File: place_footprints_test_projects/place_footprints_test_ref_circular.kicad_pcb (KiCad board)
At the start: 2 copper layers, 65 parts

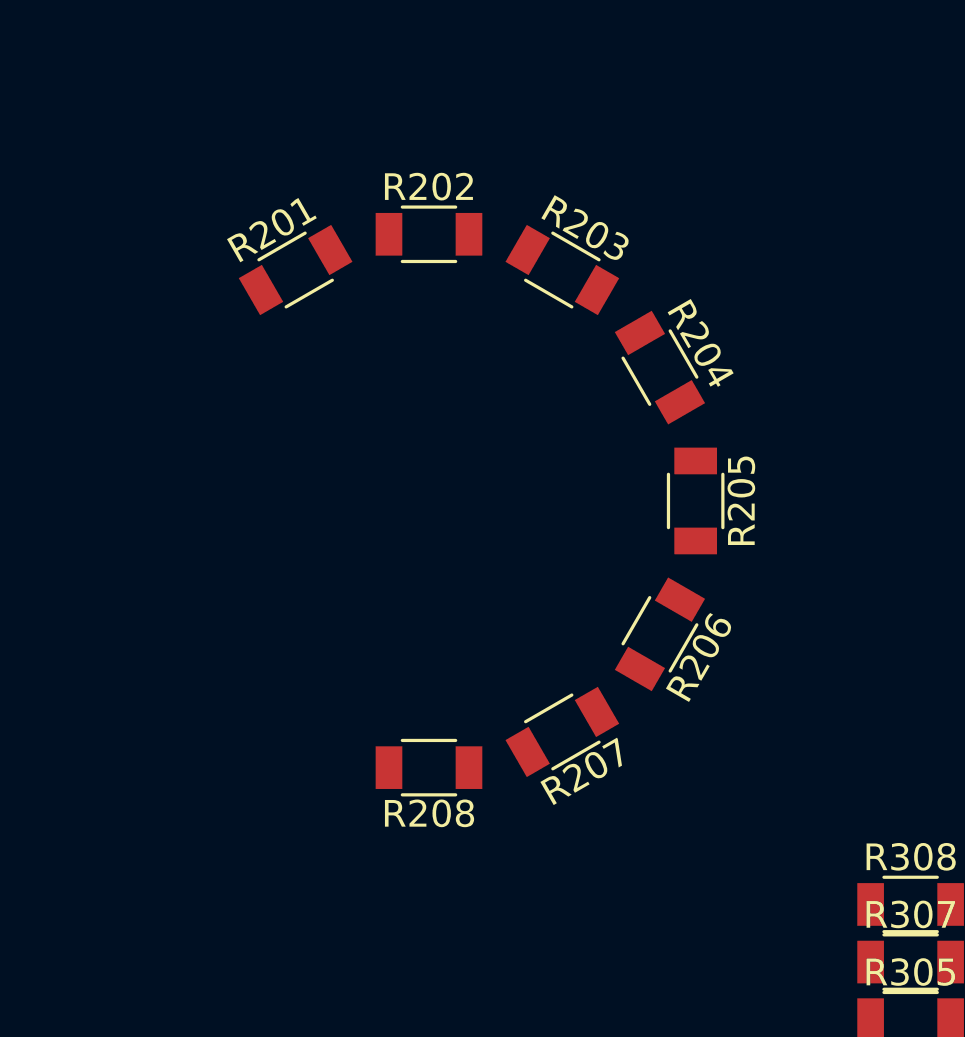
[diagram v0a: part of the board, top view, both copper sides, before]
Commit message: Update make_a_package.sh
Support footprint text placement and rotation

Add support for footprint text placement and rotation
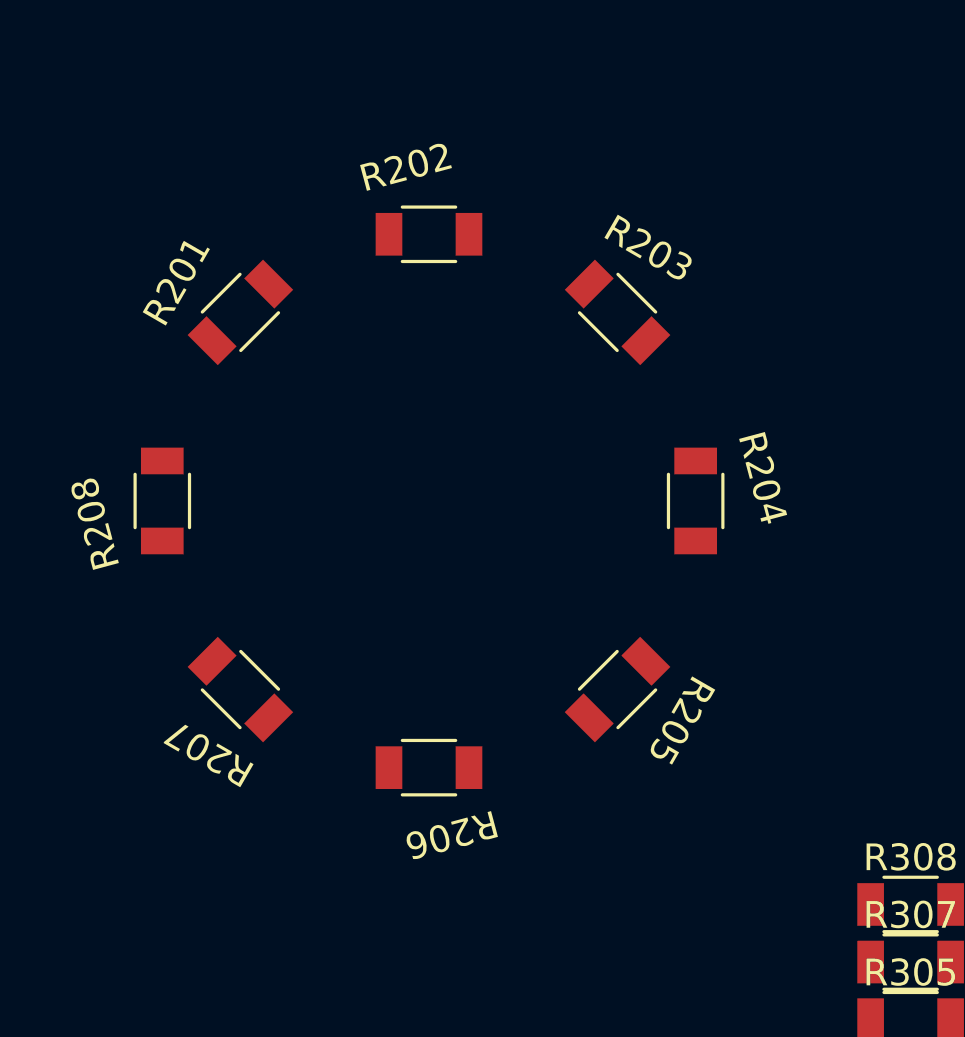
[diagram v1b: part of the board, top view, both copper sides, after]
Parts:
- moved R208 14.1 mm to (32.0, 44.0), turned to 90 degrees
- moved R207 12.2 mm to (34.9, 51.1), turned to 135 degrees
- moved R206 10.00 mm to (42.0, 54.0), turned to 180 degrees
- moved R205 7.65 mm to (49.1, 51.1), turned to -135 degrees
- moved R204 5.18 mm to (52.0, 44.0), turned to -90 degrees
- moved R201 2.61 mm to (34.9, 36.9), turned to 45 degrees
- moved R203 2.61 mm to (49.1, 36.9), turned to -45 degrees

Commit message: update test project
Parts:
- added R101: R, Resistor_SMD:R_1210_3225Metric_Pad1.30x2.65mm_HandSolder, F.Cu at (110.5, 71.1)
- R301, R601: moved to B.Cu
- moved R403 39.9 mm to (48.8, 70.2)
- moved R405 39.9 mm to (48.8, 72.4)
- moved R406 39.9 mm to (53.3, 70.2)
- moved R407 39.9 mm to (48.8, 74.5)
- moved R402 39.9 mm to (44.2, 72.4)
- moved R404 39.9 mm to (44.2, 74.5)
- moved R408 39.9 mm to (53.3, 72.4)
- moved R301 1.72 mm to (69.8, 62.9), turned to -170 degrees
- moved R601 1.66 mm to (87.0, 62.9), turned to 170 degrees
- turned R204 to -75 degrees
- turned R205 to -120 degrees
- turned R206 to -165 degrees
- turned R207 to 165 degrees
- turned R208 to 120 degrees
